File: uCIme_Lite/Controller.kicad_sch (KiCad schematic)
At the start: 8 parts

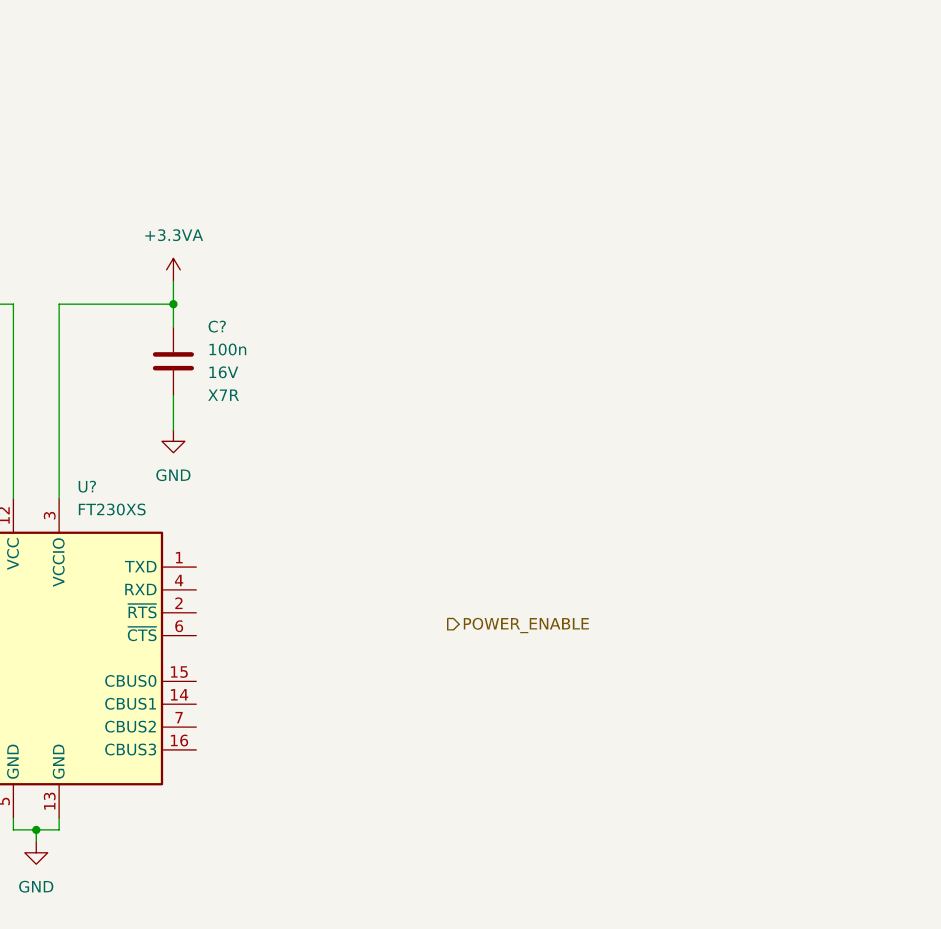
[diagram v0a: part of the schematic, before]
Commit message: lite: Added serial and USB connectors. A voltage translator is provided on the serial ports for the user to select the appropriate board voltage. No voltage translator is provided on the FTDI GPIO pins because they are meant to be used with custom extension boards.
Signed-off-by: Adrien Ricciardi <aricciardi@baylibre.com>
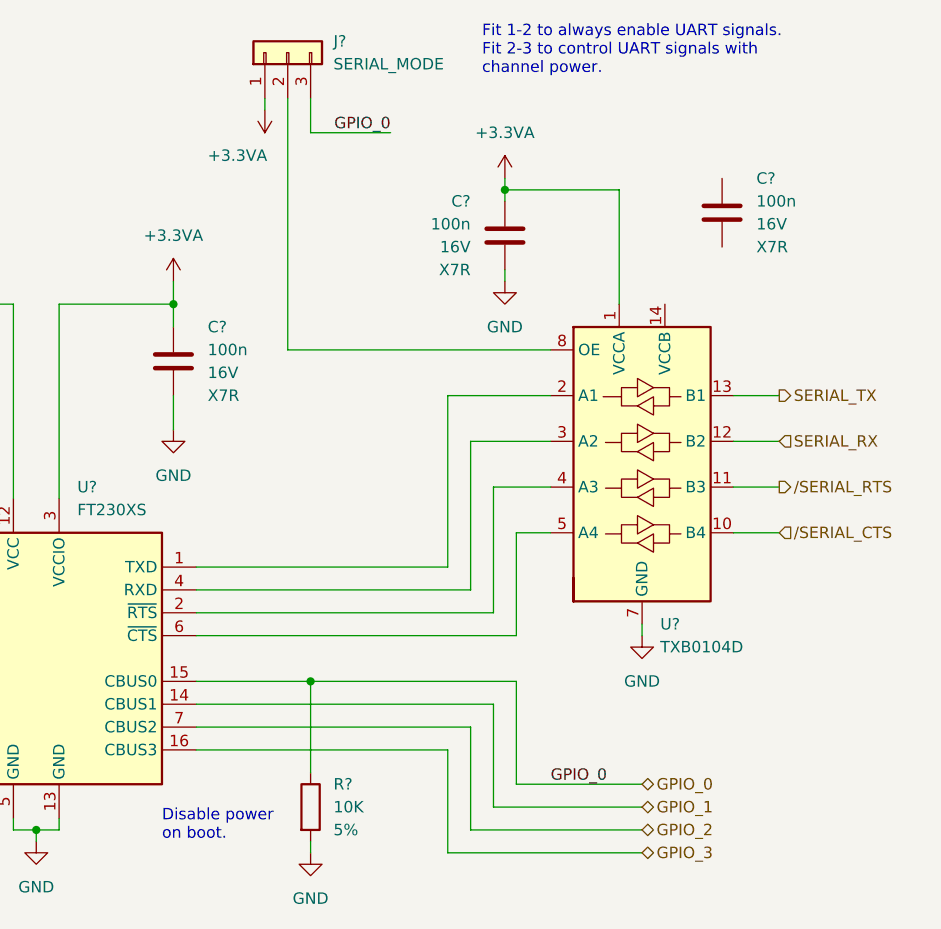
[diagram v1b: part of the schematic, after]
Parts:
- added C? (x2): 100n, Capacitor_SMD:C_0603_1608Metric, symbol Device:C
- added J?: SERIAL_MODE, symbol Connector_Generic:Conn_01x03
- added R?: 10K, Resistor_SMD:R_0603_1608Metric, symbol Device:R
- added U?: TXB0104D, Package_SO:SOIC-14_3.9x8.7mm_P1.27mm, symbol Logic_LevelTranslator:TXB0104D
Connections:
- net +3.3VA: now also C?.1, J?.1 (Pin_1), U?.1 (VCCA)
- net GND: now also C?.2, R?.2, U?.7 (GND)
- net at U?.1 (TXD): now also U?.2 (A1)
- net GPIO_1: now reaches U?.14 (CBUS1)
- net GPIO_0: now reaches U?.15 (CBUS0)
- net GPIO_0: now also J?.3 (Pin_3), R?.1
- net GPIO_3: now reaches U?.16 (CBUS3)
- net at U?.2 (~{RTS}): now also U?.4 (A3)
- net at U?.4 (RXD): now also U?.3 (A2)
- net at U?.6 (~{CTS}): now also U?.5 (A4)
- net GPIO_2: now reaches U?.7 (CBUS2)
- new net: J?.2 (Pin_2), U?.8 (OE)
- new net SERIAL_RX: U?.12 (B2)
- new net SERIAL_TX: U?.13 (B1)
- new net /SERIAL_CTS: U?.10 (B4)
- new net /SERIAL_RTS: U?.11 (B3)
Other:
- note added: "Disable power on boot."
- note added: "Fit 1-2 to always enable UART signals. Fit 2-3 to control UART signals with channel power."

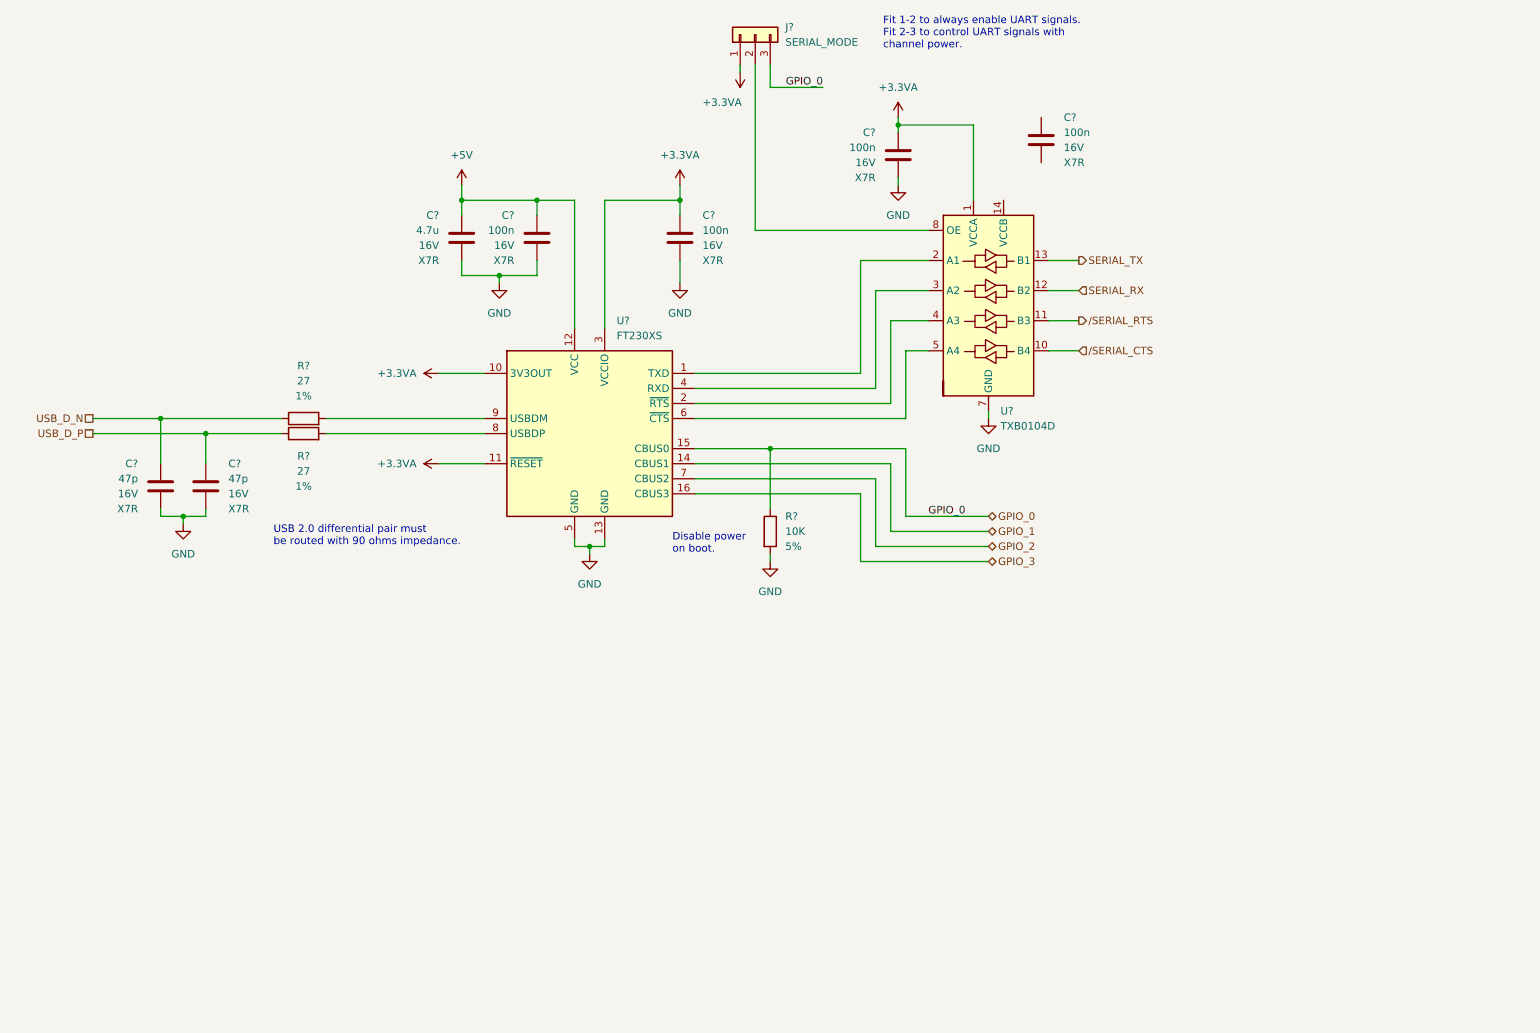
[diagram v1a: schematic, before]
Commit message: lite: Added the LDOs for the serial port voltage translator.
Signed-off-by: Adrien Ricciardi <aricciardi@baylibre.com>
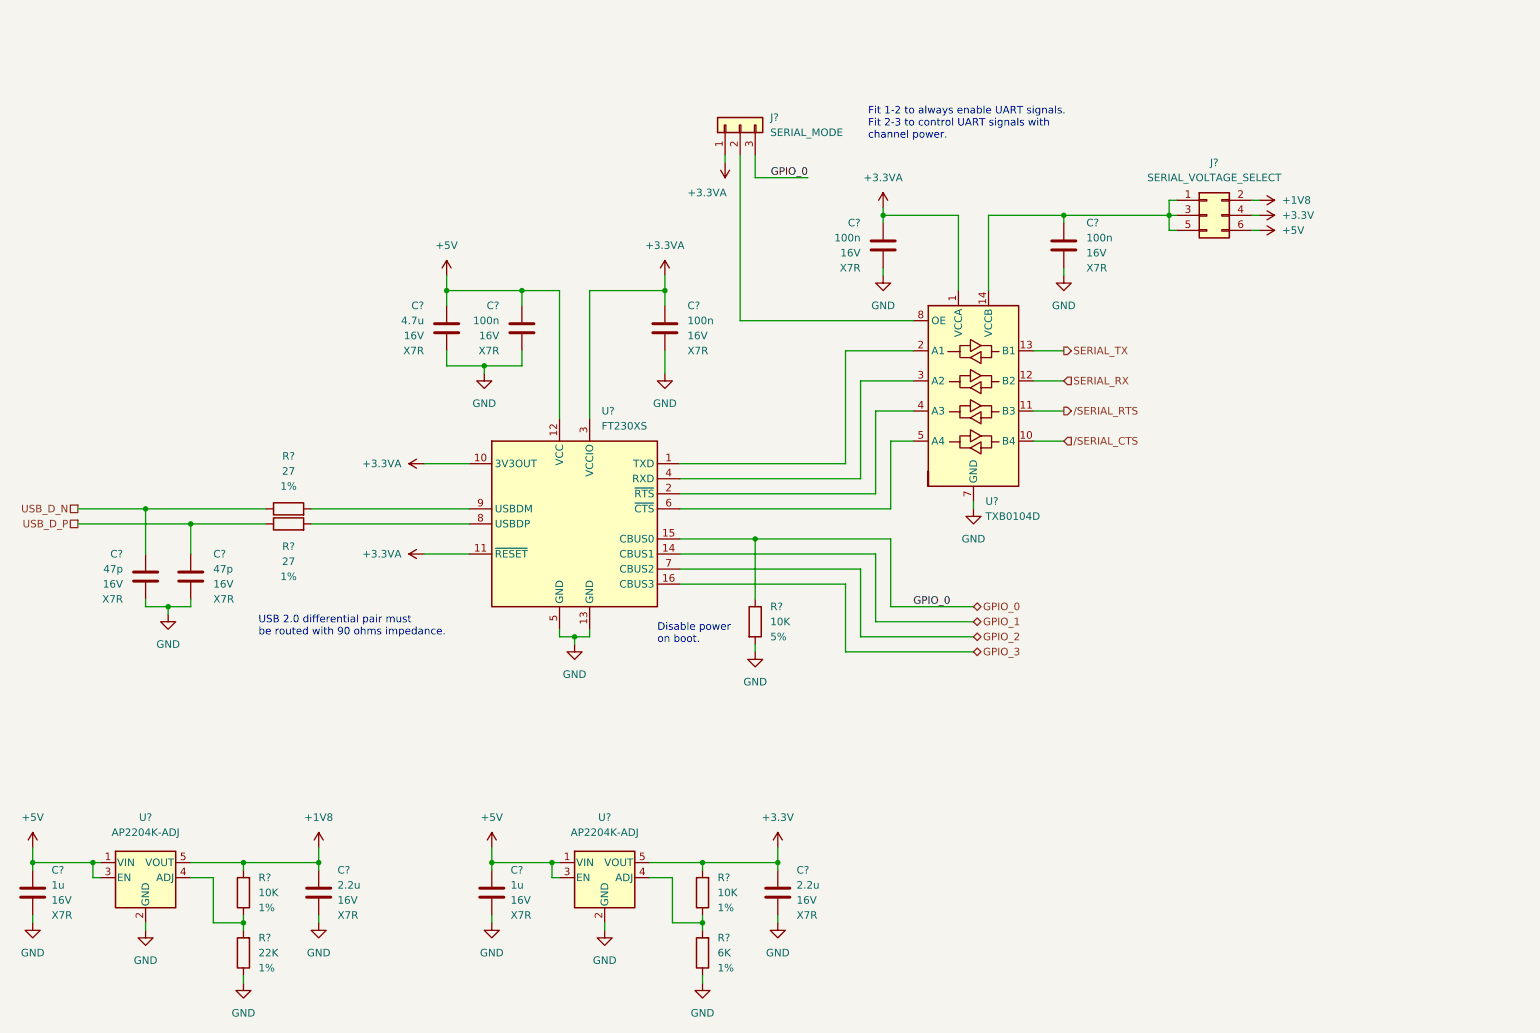
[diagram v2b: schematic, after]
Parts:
- added C? (x2): 2.2u, Capacitor_SMD:C_0603_1608Metric, symbol Device:C
- added C? (x2): 1u, Capacitor_SMD:C_0603_1608Metric, symbol Device:C
- added J?: SERIAL_VOLTAGE_SELECT, symbol Connector_Generic:Conn_02x03_Odd_Even
- added R?: 22K, Resistor_SMD:R_0603_1608Metric, symbol Device:R
- added R? (x2): 10K, Resistor_SMD:R_0603_1608Metric, symbol Device:R
- added R?: 6K, Resistor_SMD:R_0603_1608Metric, symbol Device:R
- added U? (x2): AP2204K-ADJ, Package_TO_SOT_SMD:SOT-23-5, symbol Regulator_Linear:AP2204K-ADJ
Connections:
- net +5V: now also C?.1, C?.1, J?.6 (Pin_6), U?.1 (VIN), U?.1 (VIN), U?.3 (EN), U?.3 (EN)
- net GND: now also C?.2, C?.2, C?.2, C?.2, C?.2, R?.1, R?.1, U?.2 (GND), U?.2 (GND)
- net at U?.14 (VCCB): now also C?.1, J?.1 (Pin_1), J?.3 (Pin_3), J?.5 (Pin_5)
- new net: R?.1, R?.2, U?.4 (ADJ) (x2)
- new net +1V8: C?.1, J?.2 (Pin_2), R?.2, U?.5 (VOUT)
- new net +3.3V: C?.1, J?.4 (Pin_4), R?.2, U?.5 (VOUT)
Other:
- moved on the sheet: C?, J?, R?, U?

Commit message: lite: Added jumpers to control the power channel mode (always enabled, always disabled or controlled by a FTDI GPIO).
Signed-off-by: Adrien Ricciardi <aricciardi@baylibre.com>
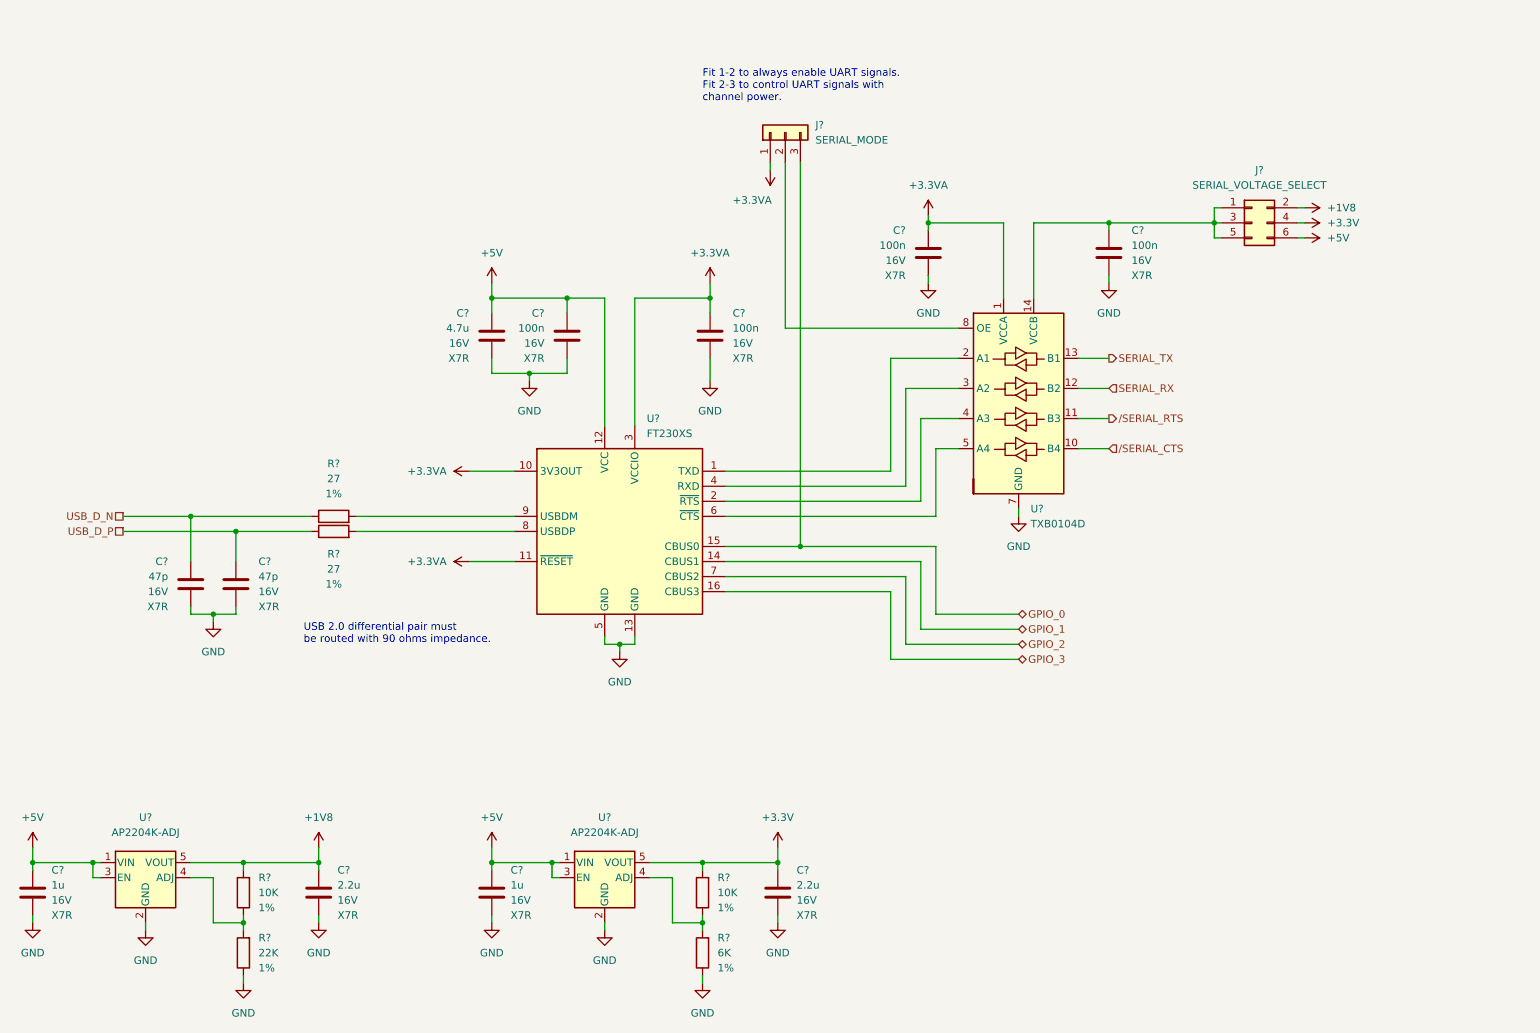
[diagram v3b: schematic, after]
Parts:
- removed R?: 10K, Resistor_SMD:R_0603_1608Metric, symbol Device:R
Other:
- note removed: "Disable power on boot."
- moved on the sheet: C?, J?, R?, U?

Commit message: lite: Added leds to schematic. One led for power switch, and two for UART TX and RX.
Signed-off-by: Adrien Ricciardi <aricciardi@baylibre.com>
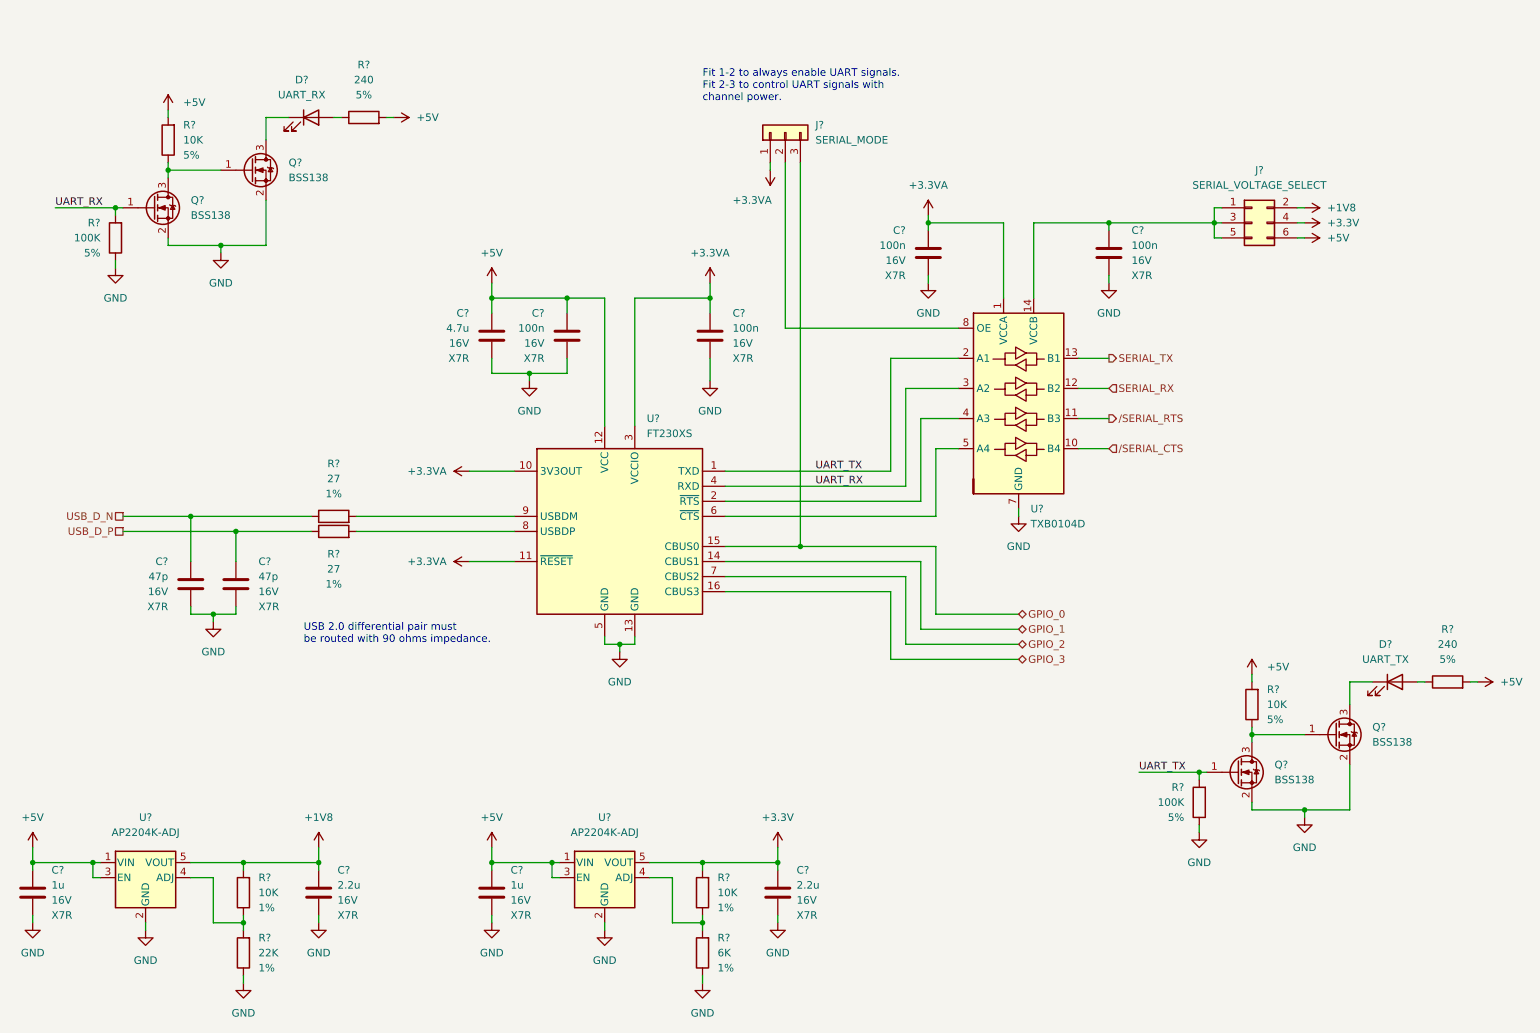
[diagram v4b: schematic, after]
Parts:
- added D?: UART_TX, symbol Device:LED
- added D?: UART_RX, symbol Device:LED
- added Q? (x4): BSS138, Package_TO_SOT_SMD:SOT-23, symbol Transistor_FET:BSS138
- added R? (x2): 240, Resistor_SMD:R_1206_3216Metric, symbol Device:R
- added R? (x2): 100K, Resistor_SMD:R_1206_3216Metric, symbol Device:R
- added R? (x2): 10K, Resistor_SMD:R_1206_3216Metric, symbol Device:R
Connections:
- net +5V: now also R?.2, R?.2, R?.2, R?.2
- net GND: now also Q?.2 (S), Q?.2 (S), Q?.2 (S), Q?.2 (S), R?.1, R?.1
- net UART_TX: now reaches U?.1 (TXD), U?.2 (A1)
- net UART_TX: now also Q?.1 (G), R?.2
- net UART_RX: now reaches U?.3 (A2), U?.4 (RXD)
- net UART_RX: now also Q?.1 (G), R?.2
- new net: Q?.1 (G), Q?.3 (D), R?.1 (x2)
- new net: D?.1 (K), Q?.3 (D) (x2)
- new net: D?.2 (A), R?.1 (x2)
